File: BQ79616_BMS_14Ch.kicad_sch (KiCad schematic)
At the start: 164 parts, among them J1 Conn_Therm, J2 Conn_02x10_Odd_Even, J3 Conn_02x10_Odd_Even, J4 BMS_A_OUT, J5 BMS_A_IN, Q1 MMBT5551

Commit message: Save for further try on re-configure of pin position
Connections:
- net CELL_A1: now also J3.12 (Pin_12); no longer J3.9 (Pin_9)
- net CELL_A2: now also J3.9 (Pin_9); no longer J3.8 (Pin_8)
- net CELL_A3: now also J3.8 (Pin_8); no longer J3.5 (Pin_5)
- net CELL_A4: now also J3.5 (Pin_5); no longer J3.4 (Pin_4)
- net CELL_A5: now also J3.4 (Pin_4); no longer J3.1 (Pin_1)
- net CELL_A6: now also J3.1 (Pin_1); no longer J2.17 (Pin_17)
- net CVDD_A: now also J3.20 (Pin_20)
- net GND1: now also J3.13 (Pin_13); no longer J3.12 (Pin_12)
- net RX_A: now also J3.16 (Pin_16); no longer J3.13 (Pin_13)
- net TX_A: now also J3.17 (Pin_17)
- net at TR2.1: now also R55.2; no longer R54.2
- net at TR2.3: now also R54.2; no longer R55.2
- net at TR2.4: now also J5.1 (Pin_1); no longer J5.2 (Pin_2)
- net at TR2.6: now also J5.2 (Pin_2); no longer J5.1 (Pin_1)
- net COMHN_A renamed COMHN
- net COMHP_A renamed COMHP
- net COMLN_A renamed COMLN
- net COMLP_A renamed COMLP
- no-connect marks 30 -> 32
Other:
- moved on the sheet: C47, C48, C49, C50, C51, C52, J2, J4, J5, R50, R51, R52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

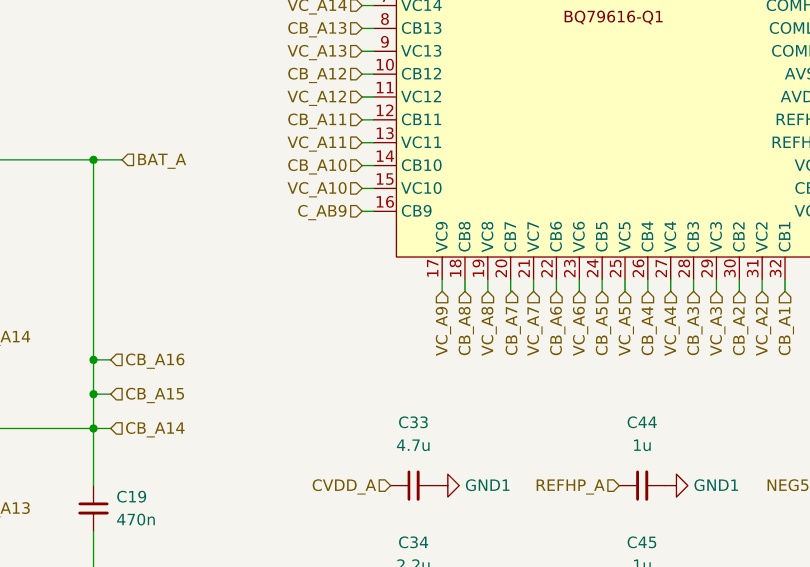
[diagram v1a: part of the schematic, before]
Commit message: Finish layout for basic need, waited to add logos and labels
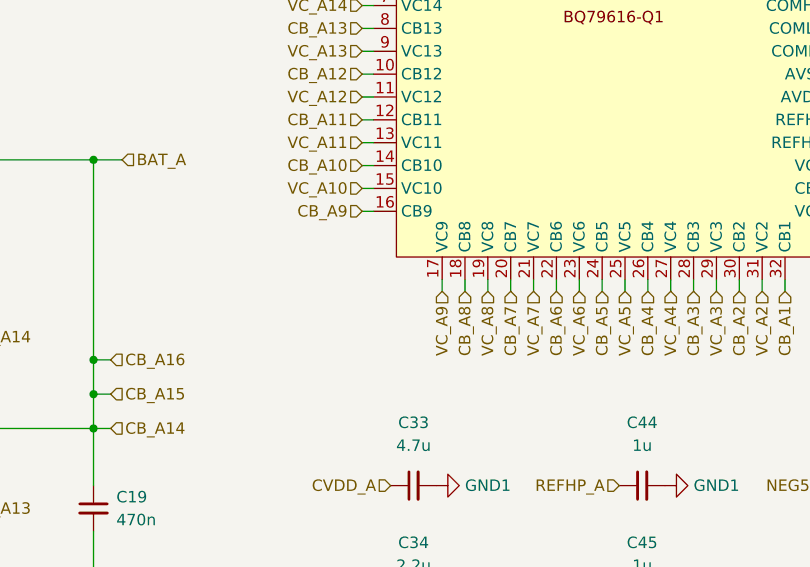
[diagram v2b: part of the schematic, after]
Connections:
- net C_AB9 is gone; now on net CB_A9: U1.16 (CB9)
- net CB_A7: now also U1.20 (CB7)
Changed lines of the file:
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@@
     (effects (font (size 1.27 1.27)) (justify right))
   )
-  (hierarchical_label "CB_A7" (shape input) (at 136.6624 82.5338 270) (fields_autoplaced)
+  (hierarchical_label "CB_A7" (shape input) (at 136.525 82.55 270) (fields_autoplaced)
     (effects (font (size 1.27 1.27)) (justify right))
   )
@@
     (effects (font (size 1.27 1.27)) (justify left))
   )
-  (hierarchical_label "C_AB9" (shape input) (at 120.015 73.66 180) (fields_autoplaced)
+  (hierarchical_label "CB_A9" (shape input) (at 120.015 73.66 180) (fields_autoplaced)
     (effects (font (size 1.27 1.27)) (justify right))
   )

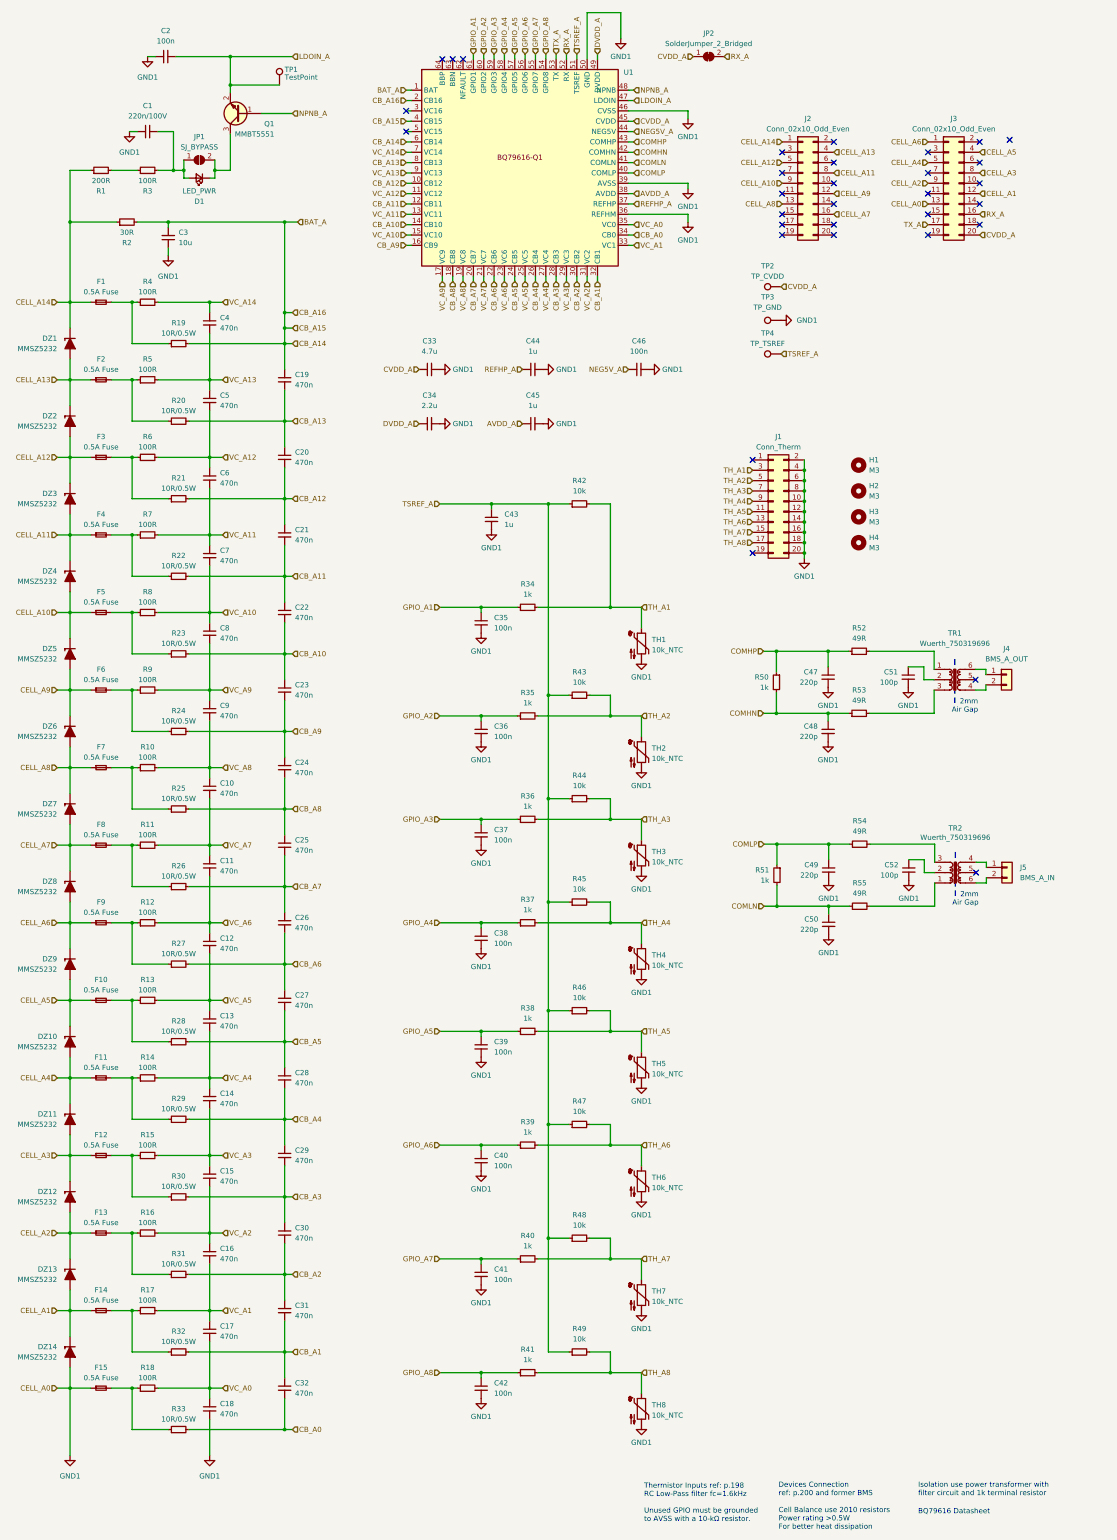
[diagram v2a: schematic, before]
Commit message: BMS v0.0.2
Use external FET for balancing
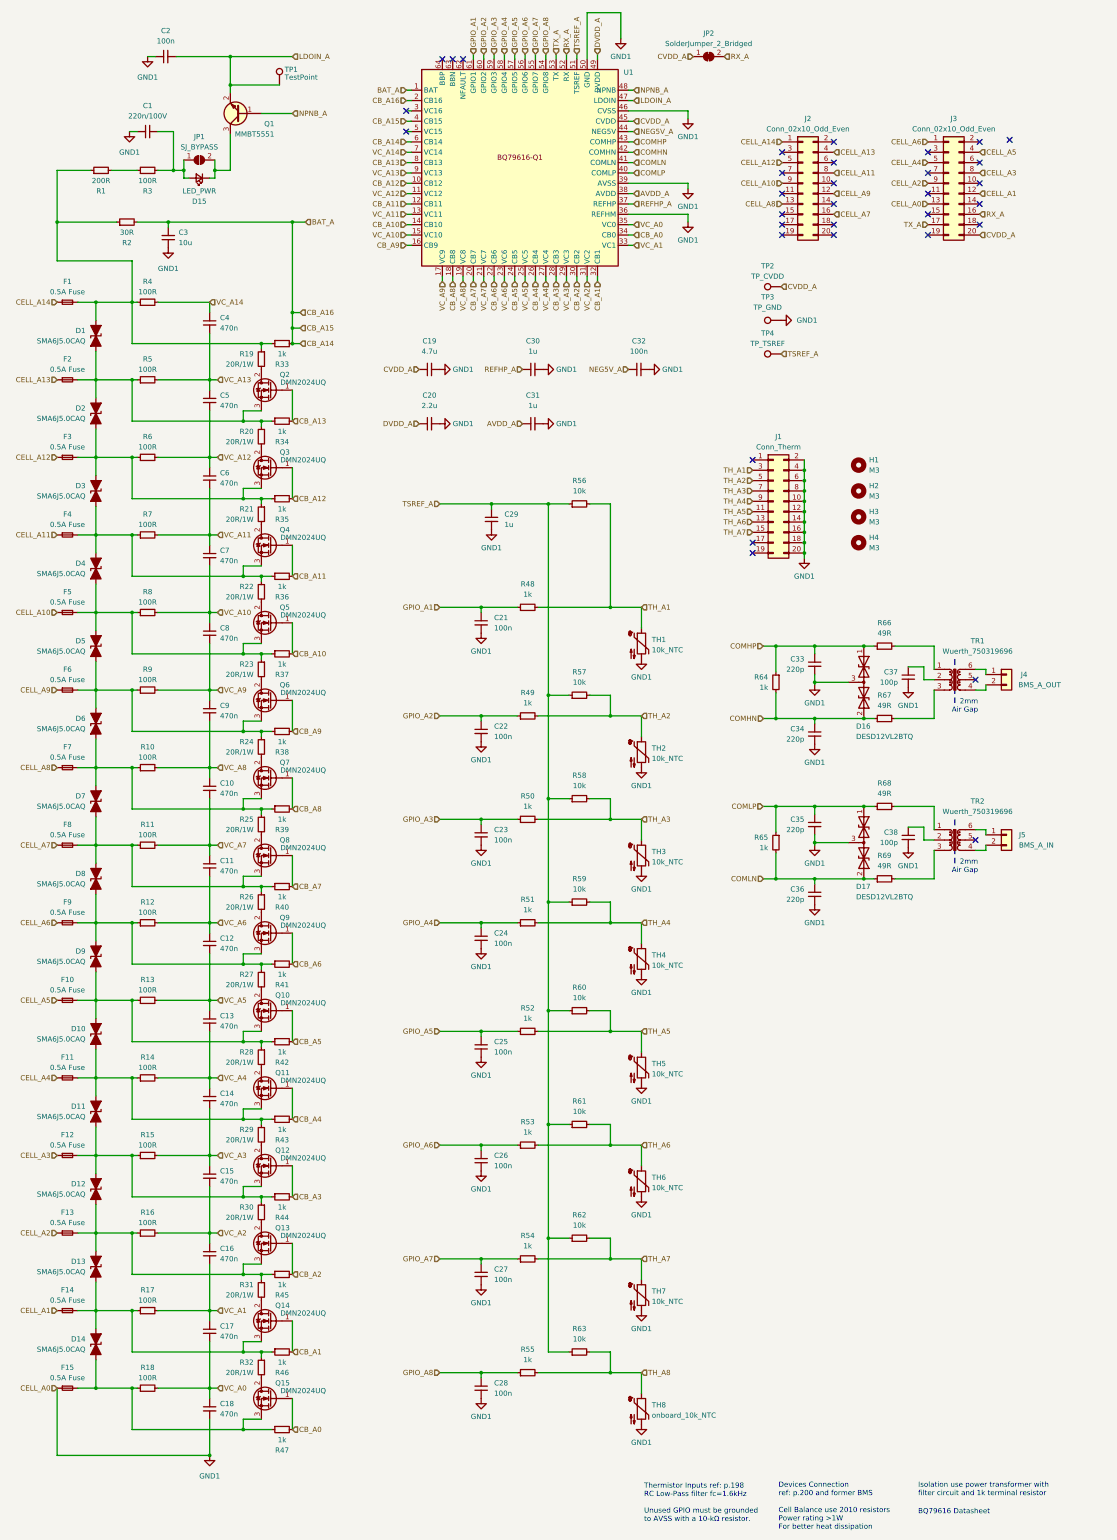
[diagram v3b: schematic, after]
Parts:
- removed C19, C20, C21, C22, C23, C24, C25, C26, C27, C28, C29, C30, C31, C32: 470n, Capacitor_SMD:C_0603_1608Metric, symbol Device:C_Small
- removed C49, C50: 220p, Capacitor_SMD:C_0603_1608Metric, symbol Device:C_Small
- removed C52: 100p, Capacitor_SMD:C_0603_1608Metric, symbol Device:C_Small
- removed DZ1, DZ10, DZ11, DZ12, DZ13, DZ14, DZ2, DZ3, DZ4, DZ5, DZ6, DZ7, DZ8, DZ9: MMSZ5232, Diode_SMD:D_SOD-123, symbol PCM_Diode_Zener_AKL:MMSZ5232
- removed R51: 1k, Resistor_SMD:R_0603_1608Metric, symbol Device:R_Small
- removed R54, R55: 49R, Resistor_SMD:R_0603_1608Metric, symbol Device:R_Small
- added C35, C36: 220p, Capacitor_SMD:C_0603_1608Metric, symbol Device:C_Small
- added C38: 100p, Capacitor_SMD:C_0603_1608Metric, symbol Device:C_Small
- added D1, D10, D11, D12, D13, D14, D2, D3, D4, D5, D6, D7, D8, D9: SMA6J5.0CAQ, Diode_SMD:D_SMA, symbol Device:D_TVS_Filled
- added D16, D17: DESD12VL2BTQ, Package_TO_SOT_SMD:SOT-23, symbol Device:D_TVS_Dual_AAC
- added Q10, Q11, Q12, Q13, Q14, Q15, Q2, Q3, Q4, Q5, Q6, Q7, Q8, Q9: DMN2024UQ, Package_TO_SOT_SMD:SOT-23, symbol Device:Q_NMOS_GDS
- added R34, R35, R36, R37, R38, R39, R40, R41, R42, R43, R44, R45, R46, R47, R65: 1k, Resistor_SMD:R_0603_1608Metric, symbol Device:R_Small
- added R68, R69: 49R, Resistor_SMD:R_0603_1608Metric, symbol Device:R_Small
- R19, R20, R21, R22, R23, R24, R25, R26, R27, R28, R29, R30, R31, R32: value 10R/0.5W -> 20R/1W; footprint Resistor_SMD:R_2010_5025Metric -> Resistor_SMD:R_1020_2550Metric
- R33: value 10R/0.5W -> 1k; footprint Resistor_SMD:R_2010_5025Metric -> Resistor_SMD:R_0603_1608Metric
- TH8: value 10k_NTC -> onboard_10k_NTC; footprint (none) -> Resistor_SMD:R_0603_1608Metric
- renumbered C33 to C19, C34 to C20, C35 to C21, C36 to C22, C37 to C23, C38 to C24, C39 to C25, C40 to C26, C41 to C27, C42 to C28, C43 to C29, C44 to C30, C45 to C31, C46 to C32, C47 to C33, C48 to C34, C51 to C37, D1 to D15, R34 to R48, R35 to R49, R36 to R50, R37 to R51, R38 to R52, R39 to R53, R40 to R54, R41 to R55, R42 to R56, R43 to R57, R44 to R58, R45 to R59, R46 to R60, R47 to R61, R48 to R62, R49 to R63, R50 to R64, R52 to R66, R53 to R67
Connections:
- net BAT_A: now also R33.2; no longer R19.2
- net CB_A0: now also Q15.1 (G), R47.2; no longer R33.2
- net CB_A1: now also Q14.1 (G), R46.2; no longer R32.2
- net CB_A10: now also Q5.1 (G), R37.2; no longer R23.2
- net CB_A11: now also Q4.1 (G), R36.2; no longer R22.2
- net CB_A12: now also Q3.1 (G), R35.2; no longer R21.2
- net CB_A13: now also Q2.1 (G), R34.2; no longer R20.2
- net CB_A2: now also Q13.1 (G), R45.2; no longer R31.2
- net CB_A3: now also Q12.1 (G), R44.2; no longer R30.2
- net CB_A4: now also Q11.1 (G), R43.2; no longer R29.2
- net CB_A5: now also Q10.1 (G), R42.2; no longer R28.2
- net CB_A6: now also Q9.1 (G), R41.2; no longer R27.2
- net CB_A7: now also Q8.1 (G), R40.2; no longer R26.2
- net CB_A8: now also Q7.1 (G), R39.2; no longer R25.2
- net CB_A9: now also Q6.1 (G), R38.2; no longer R24.2
- net CELL_A14: no longer R1.1, R2.1
- net COMHN: now also D16.2 (A2)
- net COMHP: now also D16.1 (A1)
- net COMLN: now also C36.1, D17.2 (A2), R65.2, R69.1
- net COMLP: now also C35.1, D17.1 (A1), R65.1, R68.1
- net GND1: now also C35.2, C36.2, C38.2, D16.3 (common), D17.3 (common)
- net TH_A8: no longer J1.17 (Pin_17)
- net at F6.2, R24.1, R9.1: now also D5.1 (A1), D6.2 (A2), Q6.3 (S), R38.1
- net at F7.2, R10.1, R25.1: now also D6.1 (A1), D7.2 (A2), Q7.3 (S), R39.1
- net at F14.2, R17.1, R32.1: now also D13.1 (A1), D14.2 (A2), Q14.3 (S), R46.1
- net at F3.2, R21.1, R6.1: now also D2.1 (A1), D3.2 (A2), Q3.3 (S), R35.1
- net at F4.2, R22.1, R7.1: now also D3.1 (A1), D4.2 (A2), Q4.3 (S), R36.1
- net at F10.2, R13.1, R28.1: now also D10.2 (A2), D9.1 (A1), Q10.3 (S), R42.1
- net at TR2.2: now also C38.1
- net at F13.2, R16.1, R31.1: now also D12.1 (A1), D13.2 (A2), Q13.3 (S), R45.1
- net at F8.2, R11.1, R26.1: now also D7.1 (A1), D8.2 (A2), Q8.3 (S), R40.1
- net at F5.2, R23.1, R8.1: now also D4.1 (A1), D5.2 (A2), Q5.3 (S), R37.1
- net at F2.2, R20.1, R5.1: now also D1.1 (A1), D2.2 (A2), Q2.3 (S), R34.1
- net at F12.2, R15.1, R30.1: now also D11.1 (A1), D12.2 (A2), Q12.3 (S), R44.1
- net at F1.2, R19.1, R4.1: now also R1.1, R2.1, R33.1, D1.2 (A2)
- net at F9.2, R12.1, R27.1: now also D8.1 (A1), D9.2 (A2), Q9.3 (S), R41.1
- net at F11.2, R14.1, R29.1: now also D10.1 (A1), D11.2 (A2), Q11.3 (S), R43.1
- net at TR2.1: now also R68.2
- net at TR2.3: now also R69.2
- net at TR2.4: now also J5.2 (Pin_2); no longer J5.1 (Pin_1)
- net at TR2.6: now also J5.1 (Pin_1); no longer J5.2 (Pin_2)
- net at F15.2, R18.1: now also D14.1 (A1), Q15.3 (S), R47.1; no longer R33.1
- new net: Q9.2 (D), R26.2
- new net: Q4.2 (D), R21.2
- new net: Q13.2 (D), R30.2
- new net: Q6.2 (D), R23.2
- new net: Q7.2 (D), R24.2
- new net: Q3.2 (D), R20.2
- new net: Q12.2 (D), R29.2
- new net: Q5.2 (D), R22.2
- new net: Q10.2 (D), R27.2
- new net: Q2.2 (D), R19.2
- new net: Q11.2 (D), R28.2
- new net: Q15.2 (D), R32.2
- new net: Q8.2 (D), R25.2
- new net: Q14.2 (D), R31.2
- no-connect marks 32 -> 33
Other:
- note added: "Cell Balance use 2010 resistors Power rating >1W For better heat dissipation"
- note removed: "Cell Balance use 2010 resistors Power rating >0.5W For better heat dissipation"
- moved on the sheet: C33, C34, F1, F10, F11, F12, F13, F14, F15, F2, F3, F4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
